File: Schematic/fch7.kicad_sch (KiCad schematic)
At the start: 0 parts

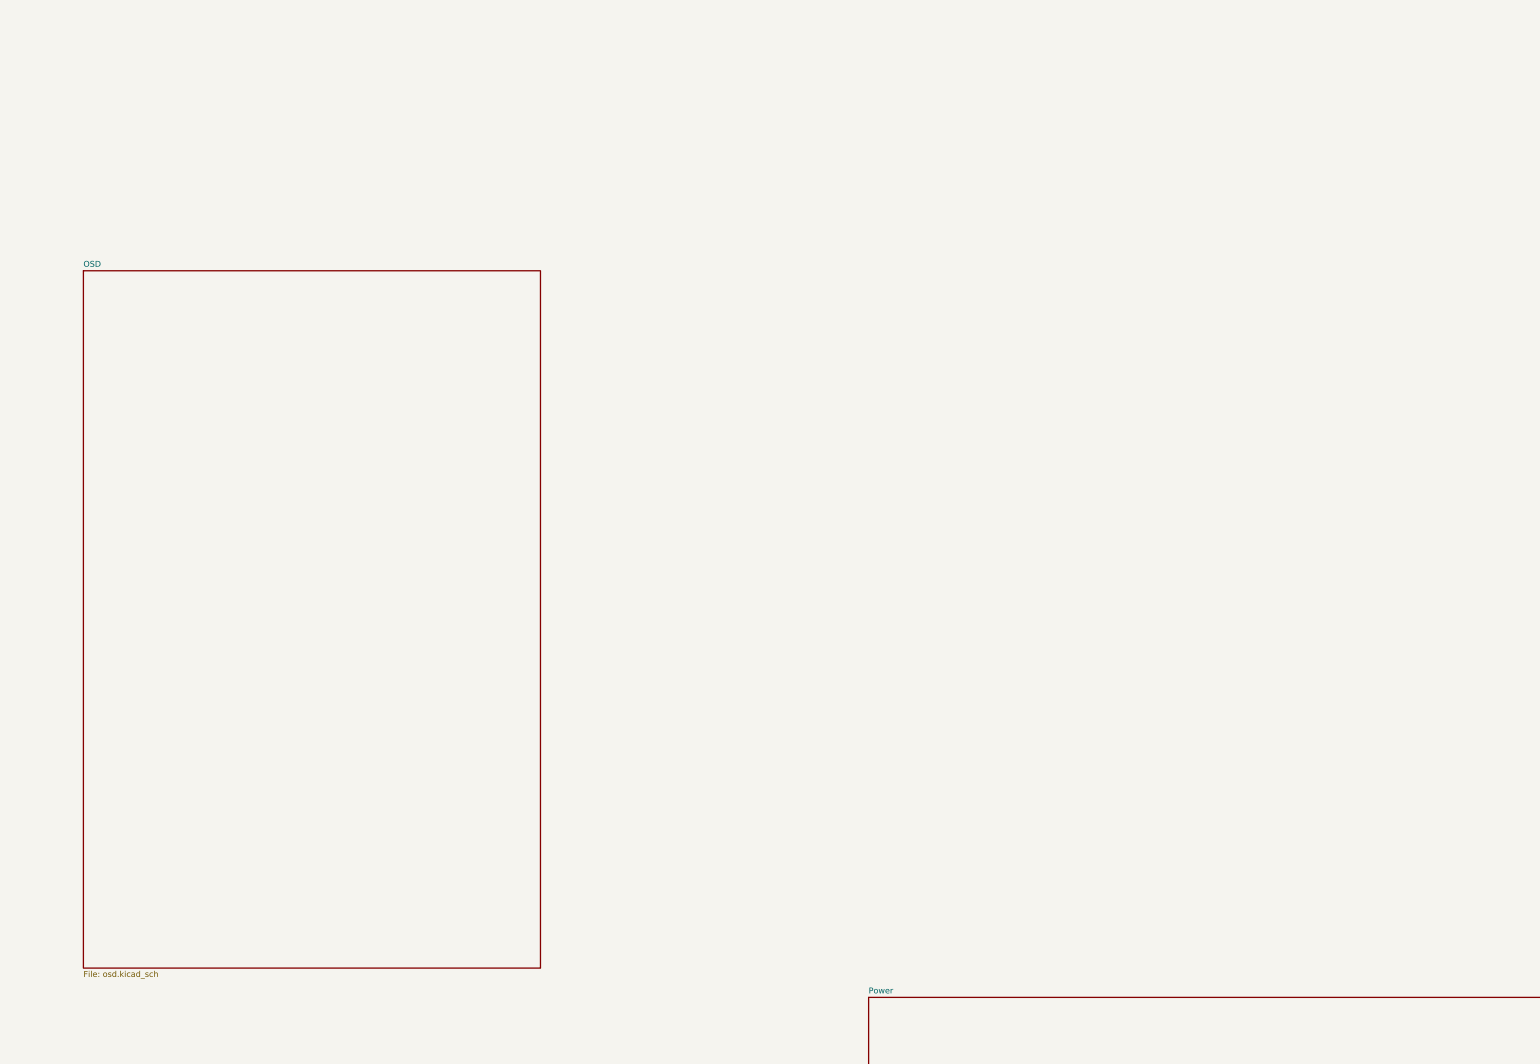
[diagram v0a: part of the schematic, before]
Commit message: Removed useless analog OSD and VTX conneections to support only digital DJI
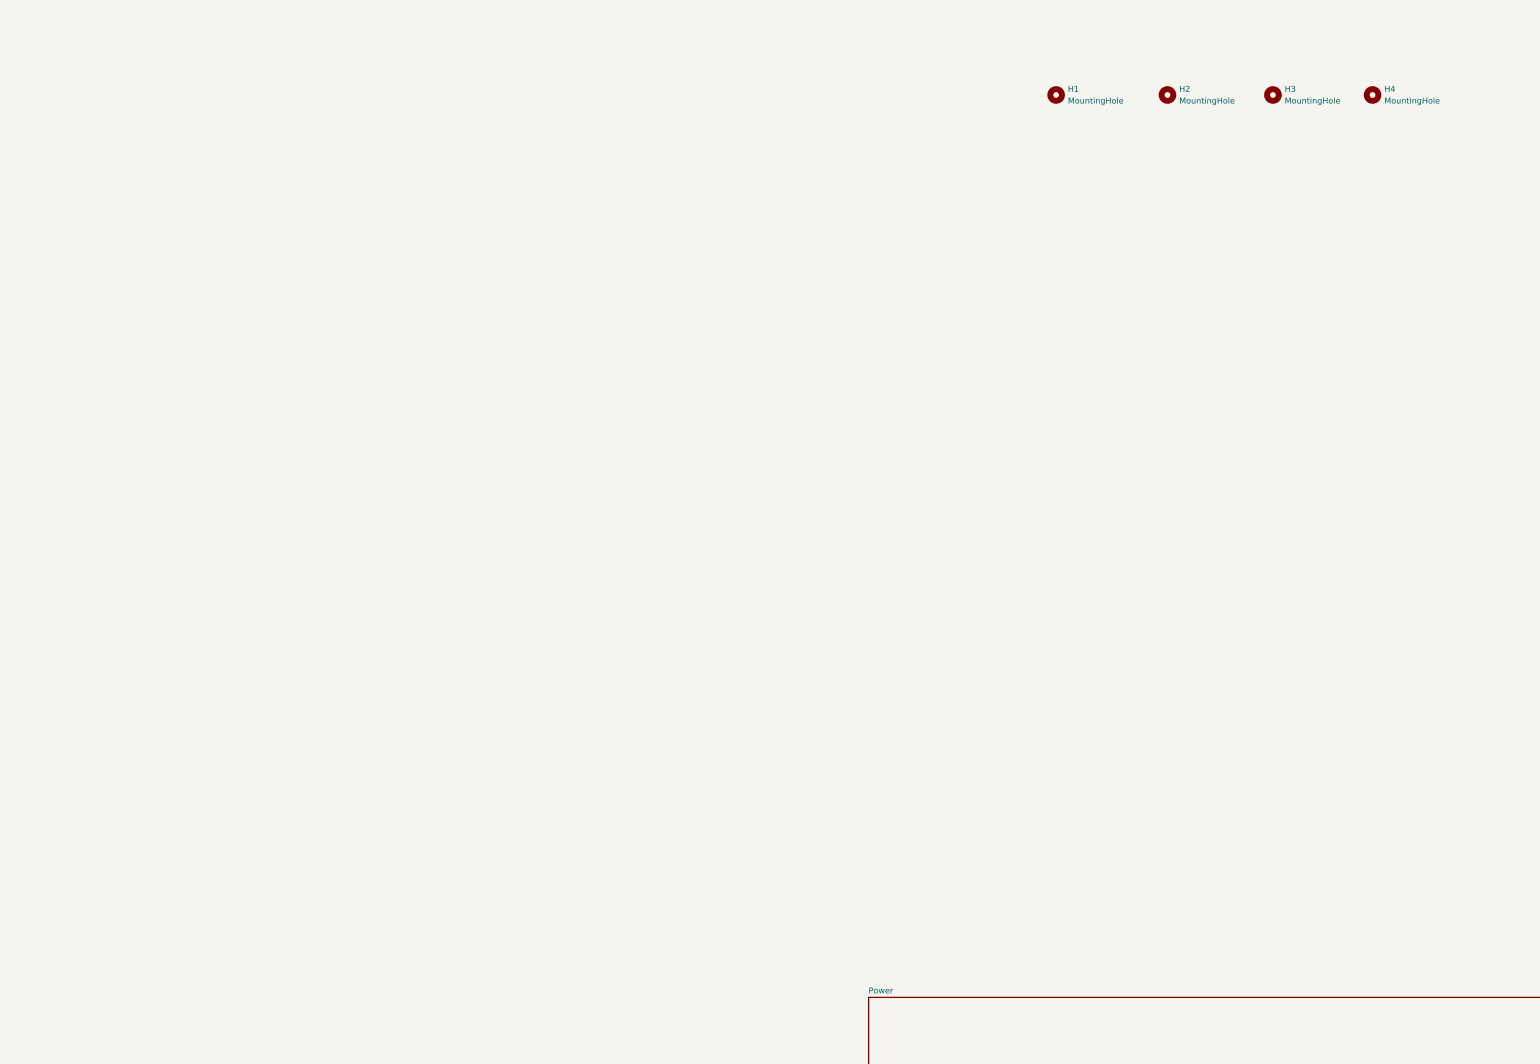
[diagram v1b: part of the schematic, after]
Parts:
- added H1, H2, H3, H4: MountingHole, MountingHole:MountingHole_3.2mm_M3, symbol Mechanical:MountingHole
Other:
- removed sheet OSD

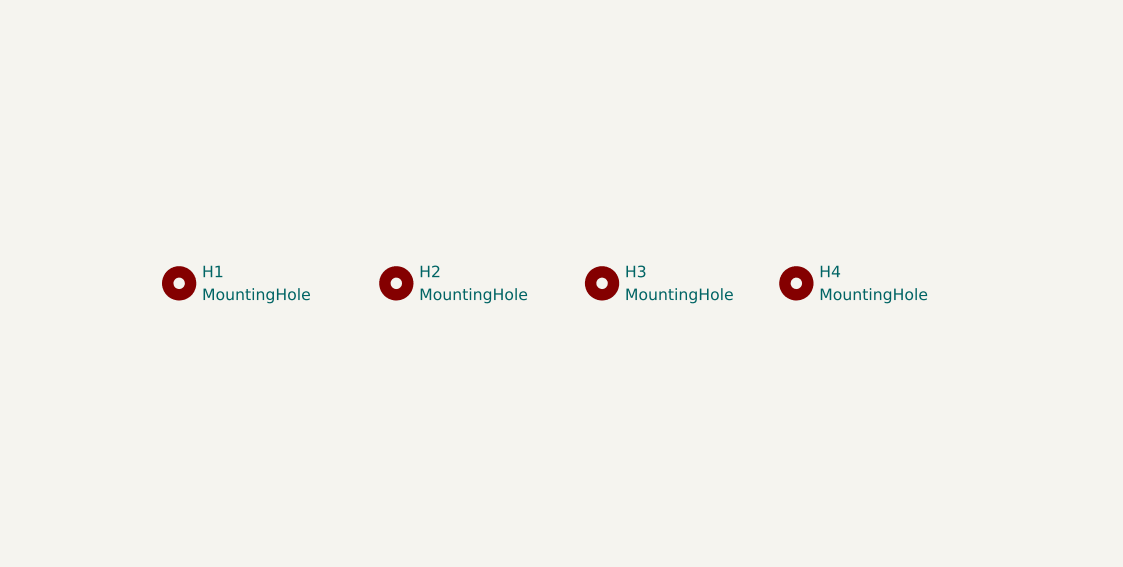
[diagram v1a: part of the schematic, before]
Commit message: Refactor mounting hole footprints and update schematic
- Deleted obsolete mounting hole footprints from the PCB design.
- Introduced a new footprint "MountingHole_quad_30.5x30.5" for improved layout.
- Updated references in the schematic to use the new mounting hole footprint.
- Adjusted positions of mounting hole symbols in the schematic for better alignment.
- Changed pin types for USB VBUS connections from "power_out" to "bidirectional" for accurate functionality.
- Cleaned up the footprint information cache to reflect the new footprint changes.
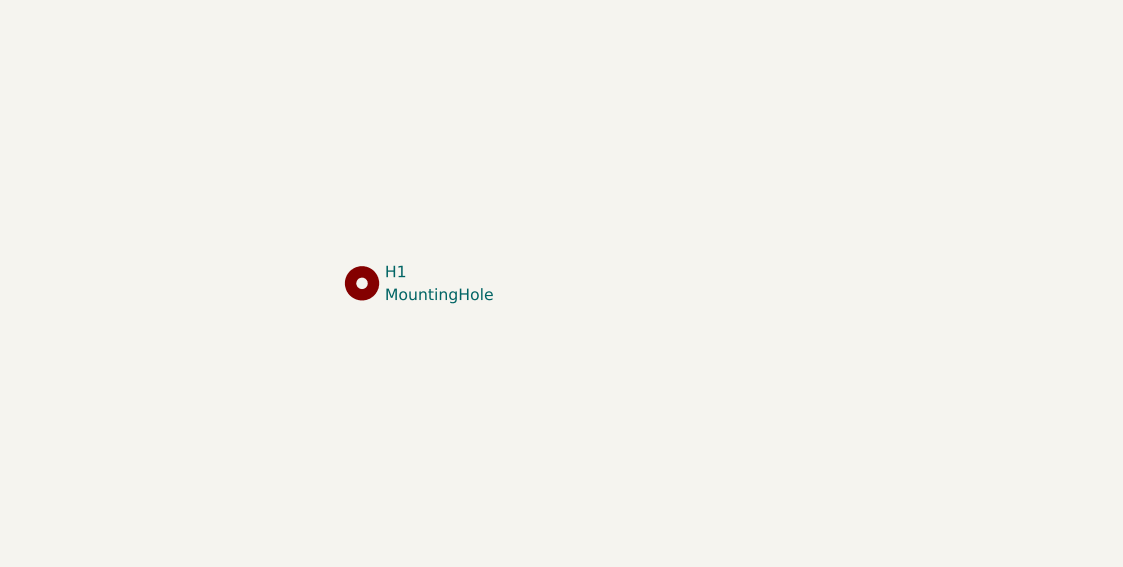
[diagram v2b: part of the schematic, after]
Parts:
- removed H2, H3, H4: MountingHole, MountingHole:MountingHole_3.2mm_M3, symbol Mechanical:MountingHole
- H1: footprint MountingHole:MountingHole_3.2mm_M3 -> fch7_fp:MountingHole_quad_30.5x30.5
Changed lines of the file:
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@@
 	(symbol
 		(lib_id "Mechanical:MountingHole")
-		(at 78.74 26.67 0)
+		(at 52.07 26.67 0)
 		(unit 1)
 		(exclude_from_sim no)
@@
 		(dnp no)
 		(fields_autoplaced yes)
-		(property "Reference" "H3"
-			(at 81.28 25.3999 0)
+		(property "Reference" "H1"
+			(at 54.61 25.3999 0)
 			(effects
 				(font
@@
 		)
 		(property "Value" "MountingHole"
-			(at 81.28 27.9399 0)
+			(at 54.61 27.9399 0)
 			(effects
 				(font
@@
 			)
 		)
-		(property "Footprint" "MountingHole:MountingHole_3.2mm_M3"
-			(at 78.74 26.67 0)
+		(property "Footprint" "fch7_fp:MountingHole_quad_30.5x30.5"
+			(at 52.07 26.67 0)
 			(effects
 				(font
@@
 		)
 		(property "Datasheet" "~"
-			(at 78.74 26.67 0)
+			(at 52.07 26.67 0)
 			(effects
 				(font
@@
 		)
 		(property "Description" "Mounting Hole without connection"
-			(at 78.74 26.67 0)
-			(effects
-				(font
-					(size 1.27 1.27)
-				)
-				(hide yes)
-			)
-		)
-		(instances
-			(project "fch7"
-				(path "/11716af6-0e6e-444b-b738-3f12da23c1a2"
-					(reference "H3")
-					(unit 1)
-				)
-			)
-		)
-	)
-	(symbol
-		(lib_id "Mechanical:MountingHole")
-		(at 55.88 26.67 0)
-		(unit 1)
-		(exclude_from_sim no)
-		(in_bom no)
-		(on_board yes)
-		(dnp no)
-		(fields_autoplaced yes)
-		(property "Reference" "H2"
-			(at 58.42 25.3999 0)
-			(effects
-				(font
-					(size 1.27 1.27)
-				)
-				(justify left)
-			)
-		)
-		(property "Value" "MountingHole"
-			(at 58.42 27.9399 0)
-			(effects
-				(font
-					(size 1.27 1.27)
-				)
-				(justify left)
-			)
-		)
-		(property "Footprint" "MountingHole:MountingHole_3.2mm_M3"
-			(at 55.88 26.67 0)
-			(effects
-				(font
-					(size 1.27 1.27)
-				)
-				(hide yes)
-			)
-		)
-		(property "Datasheet" "~"
-			(at 55.88 26.67 0)
-			(effects
-				(font
-					(size 1.27 1.27)
-				)
-				(hide yes)
-			)
-		)
-		(property "Description" "Mounting Hole without connection"
-			(at 55.88 26.67 0)
-			(effects
-				(font
-					(size 1.27 1.27)
-				)
-				(hide yes)
-			)
-		)
-		(instances
-			(project "fch7"
-				(path "/11716af6-0e6e-444b-b738-3f12da23c1a2"
-					(reference "H2")
-					(unit 1)
-				)
-			)
-		)
-	)
-	(symbol
-		(lib_id "Mechanical:MountingHole")
-		(at 31.75 26.67 0)
-		(unit 1)
-		(exclude_from_sim no)
-		(in_bom no)
-		(on_board yes)
-		(dnp no)
-		(fields_autoplaced yes)
-		(property "Reference" "H1"
-			(at 34.29 25.3999 0)
-			(effects
-				(font
-					(size 1.27 1.27)
-				)
-				(justify left)
-			)
-		)
-		(property "Value" "MountingHole"
-			(at 34.29 27.9399 0)
-			(effects
-				(font
-					(size 1.27 1.27)
-				)
-				(justify left)
-			)
-		)
-		(property "Footprint" "MountingHole:MountingHole_3.2mm_M3"
-			(at 31.75 26.67 0)
-			(effects
-				(font
-					(size 1.27 1.27)
-				)
-				(hide yes)
-			)
-		)
-		(property "Datasheet" "~"
-			(at 31.75 26.67 0)
-			(effects
-				(font
-					(size 1.27 1.27)
-				)
-				(hide yes)
-			)
-		)
-		(property "Description" "Mounting Hole without connection"
-			(at 31.75 26.67 0)
+			(at 52.07 26.67 0)
 			(effects
 				(font
@@
 					(unit 1)
 				)
-			)
-		)
-	)
-	(symbol
-		(lib_id "Mechanical:MountingHole")
-		(at 100.33 26.67 0)
-		(unit 1)
-		(exclude_from_sim no)
-		(in_bom no)
-		(on_board yes)
-		(dnp no)
-		(fields_autoplaced yes)
-		(property "Reference" "H4"
-			(at 102.87 25.3999 0)
-			(effects
-				(font
-					(size 1.27 1.27)
-				)
-				(justify left)
-			)
-		)
-		(property "Value" "MountingHole"
-			(at 102.87 27.9399 0)
-			(effects
-				(font
-					(size 1.27 1.27)
-				)
-				(justify left)
-			)
-		)
-		(property "Footprint" "MountingHole:MountingHole_3.2mm_M3"
-			(at 100.33 26.67 0)
-			(effects
-				(font
-					(size 1.27 1.27)
-				)
-				(hide yes)
-			)
-		)
-		(property "Datasheet" "~"
-			(at 100.33 26.67 0)
-			(effects
-				(font
-					(size 1.27 1.27)
-				)
-				(hide yes)
-			)
-		)
-		(property "Description" "Mounting Hole without connection"
-			(at 100.33 26.67 0)
-			(effects
-				(font
-					(size 1.27 1.27)
-				)
-				(hide yes)
-			)
-		)
-		(instances
-			(project "fch7"
-				(path "/11716af6-0e6e-444b-b738-3f12da23c1a2"
-					(reference "H4")
-					(unit 1)
-				)

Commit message: finished every routing and fix errors in DRC
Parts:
- H1: footprint fch7_fp:MountingHole_quad_30.5x30.5 -> fch7:MountingHole_quad_30.5x30.5
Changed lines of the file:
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@@
 			)
 		)
-		(property "Footprint" "fch7_fp:MountingHole_quad_30.5x30.5"
+		(property "Footprint" "fch7:MountingHole_quad_30.5x30.5"
 			(at 52.07 26.67 0)
 			(effects
